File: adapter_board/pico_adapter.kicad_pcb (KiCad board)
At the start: 2 copper layers, 47 x 55.9 mm, 2 parts, among them J1 Conn_02x05_Odd_Even, U1 Pico

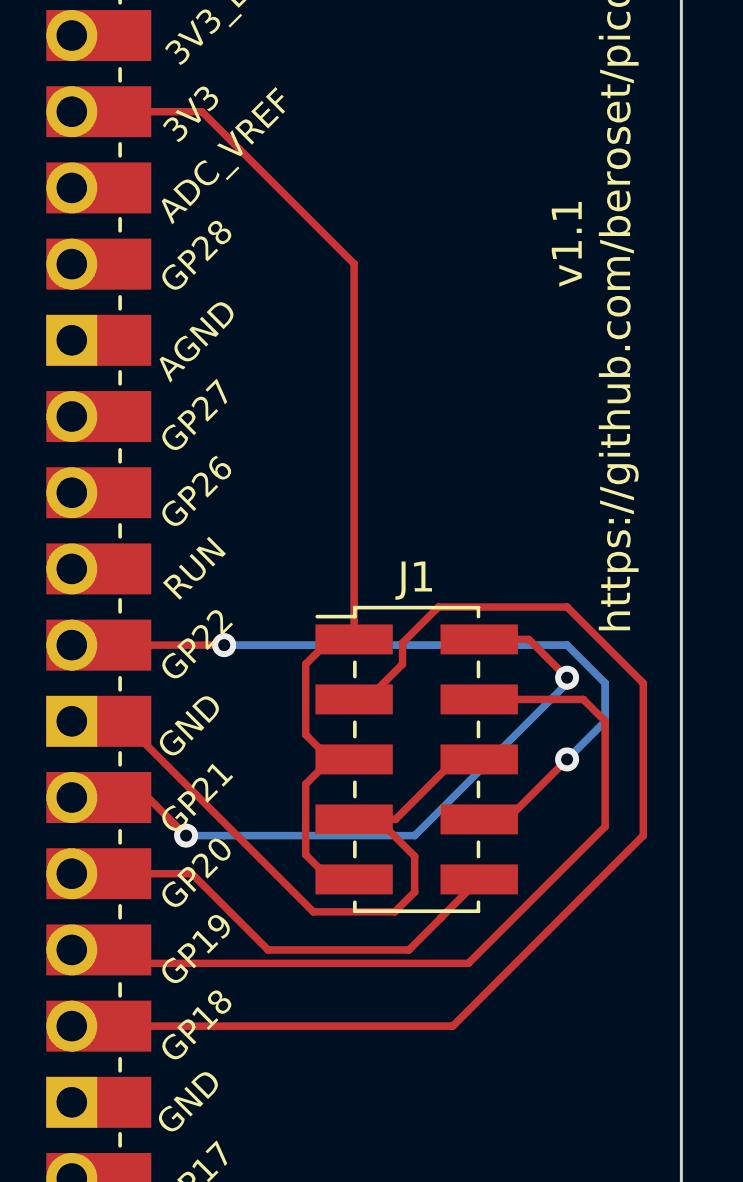
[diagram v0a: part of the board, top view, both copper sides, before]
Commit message: Add silkscreen connector pin numbers
This also updates to the latest version of KiCad, changes the default
page size to US letter and adds some details to the title block.  No
electrical changes were made.

Signed-off-by: Ed Beroset <beroset@ieee.org>
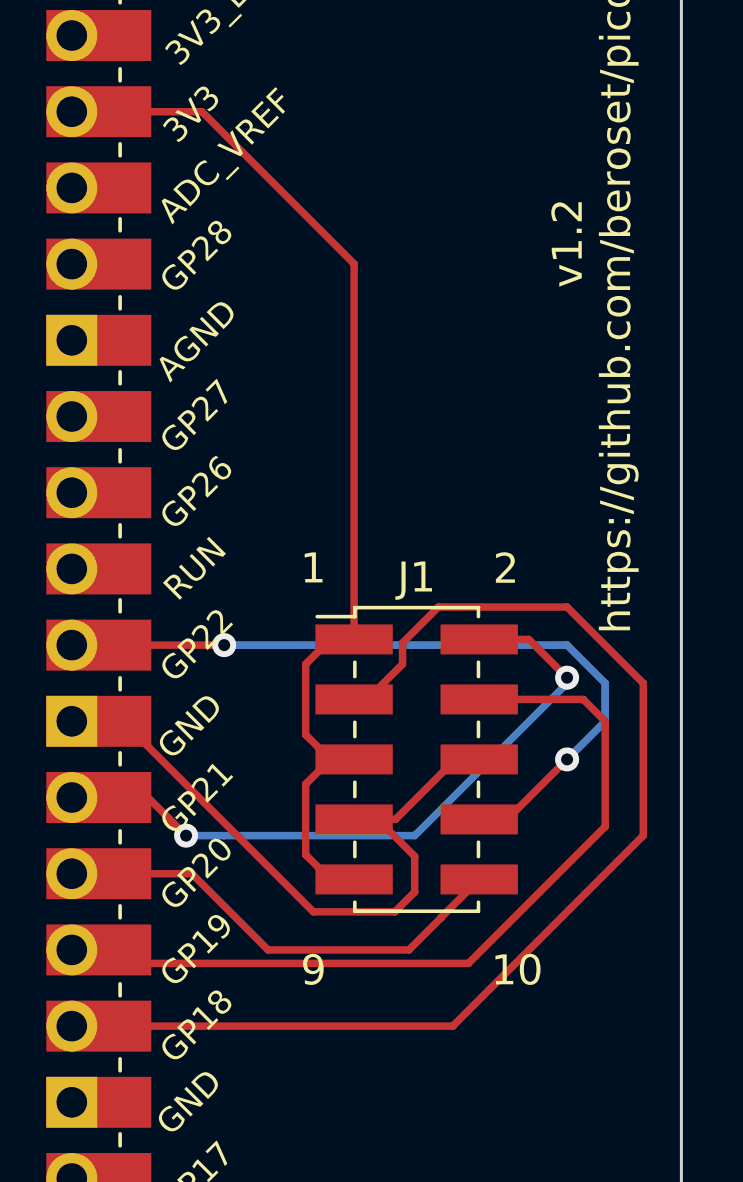
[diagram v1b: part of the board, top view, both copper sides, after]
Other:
- board text added: "1"
- board text added: "10"
- board text added: "2"
- board text added: "9"
- board text added: "v1.2 https://github.com/beroset/pico-puller"
- board text removed: "v1.1 https://github.com/beroset/pico-puller"
